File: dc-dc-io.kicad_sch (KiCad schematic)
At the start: 41 parts, among them U20 MPM54304GMN, U28 PAC1944T-E

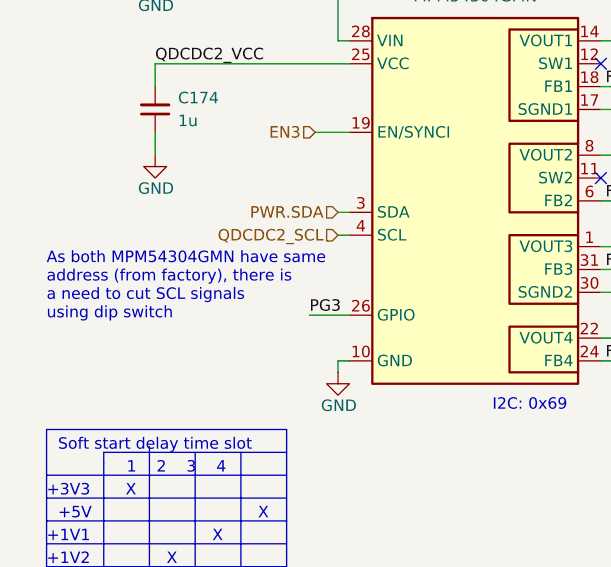
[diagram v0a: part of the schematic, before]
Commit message: [#66727] Continue routing low speed signals
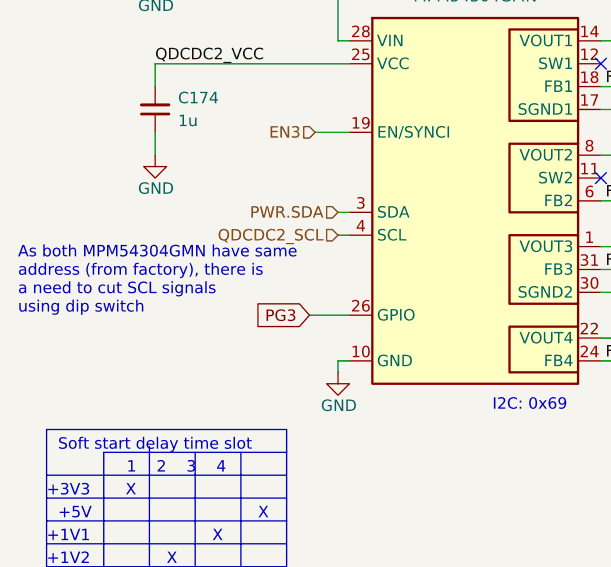
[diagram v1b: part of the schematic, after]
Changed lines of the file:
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@@
   )
   (text "As both MPM54304GMN have same \naddress (from factory), there is \na need to cut SCL signals\nusing dip switch"
-    (at 57.15 113.03 0)
+    (at 53.975 112.395 0)
     (effects (font (size 1.27 1.27)) (justify left bottom))
   )
@@
     (effects (font (size 1.27 1.27)) (justify right bottom))
   )
-  (label "PG3" (at 86.36 112.395 0) (fields_autoplaced)
-    (effects (font (size 1.27 1.27)) (justify left bottom))
-  )
   (label "5V_SEN_+" (at 149.86 174.625 180) (fields_autoplaced)
     (effects (font (size 1.27 1.27)) (justify right bottom))
@@
     (effects (font (size 1.27 1.27)) (justify left bottom))
   )
+  (global_label "PG3" (shape input) (at 86.36 112.395 180) (fields_autoplaced)
+    (effects (font (size 1.27 1.27)) (justify right))
+    (property "Intersheetrefs" "${INTERSHEET_REFS}" (at 80.2795 112.395 0)
+      (effects (font (size 1.27 1.27)) (justify right))
+    )
+  )
   (hierarchical_label "PWR.SCL" (shape input) (at 100.33 172.085 180) (fields_autoplaced)

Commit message: [#67725] Update vccio power supply
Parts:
- C193: DNP DNP -> (none)
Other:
- note added: "1"
- note added: "Current sense monitor"
- note removed: "1 2 3 4"
- moved on the sheet: C173, C174, C178, C184, C185, C190, C191, C192, C193, C206, R145, R146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

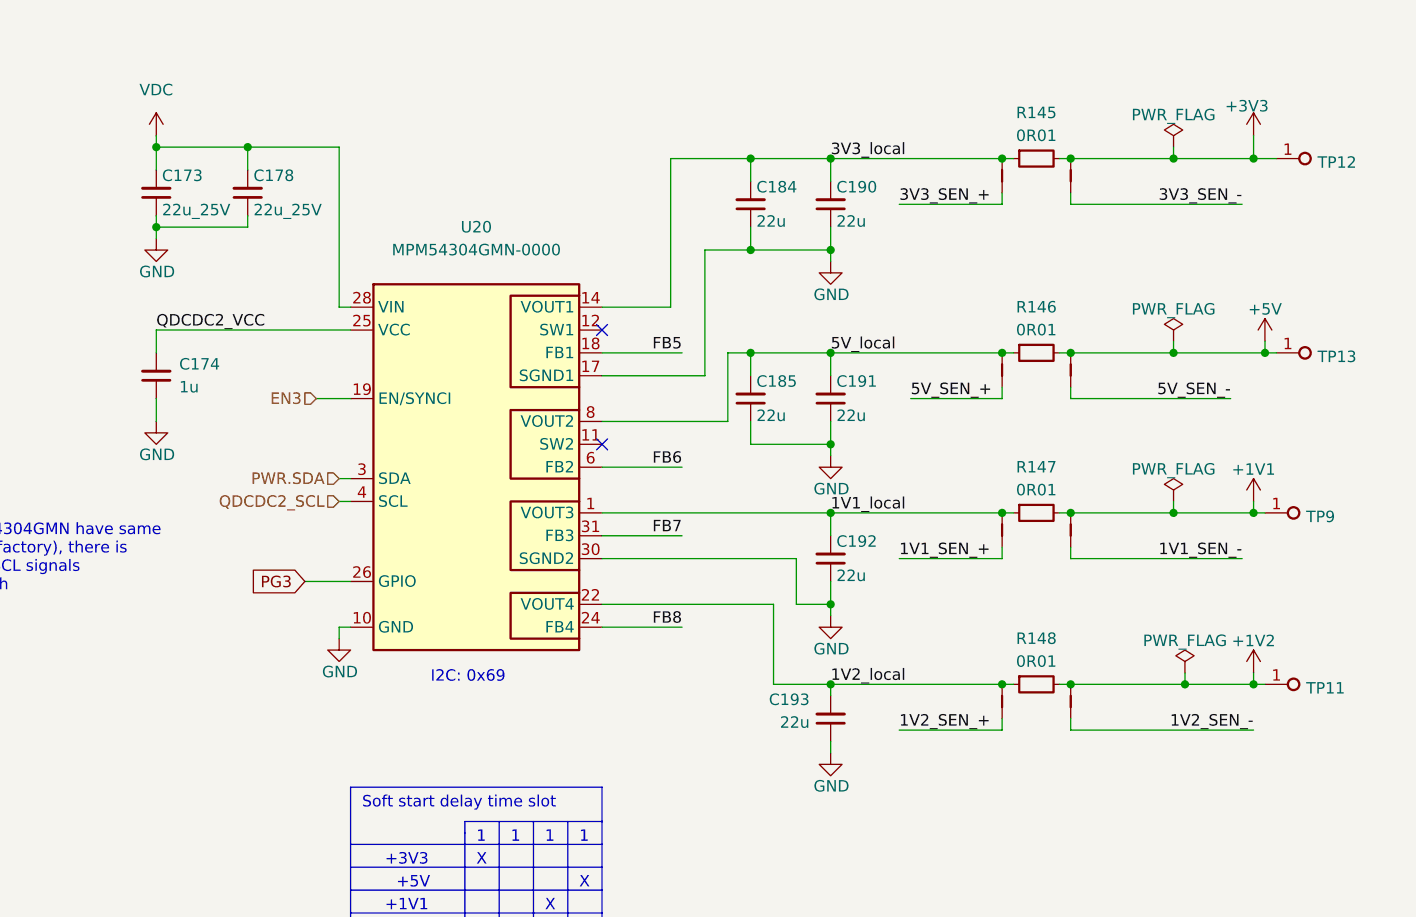
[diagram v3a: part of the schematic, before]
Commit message: [#68016] Solve ERC warrings and errors
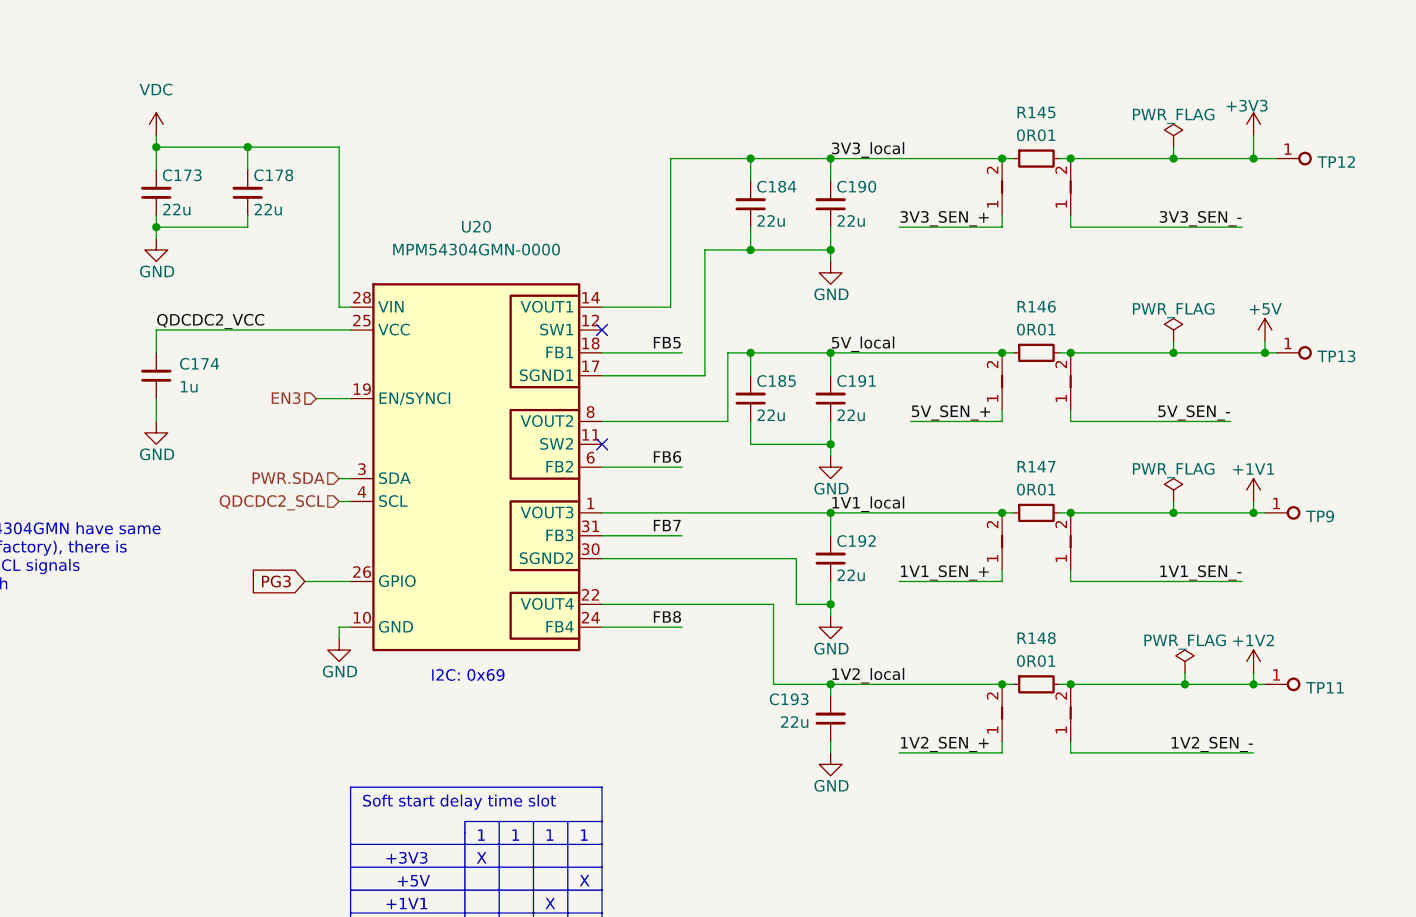
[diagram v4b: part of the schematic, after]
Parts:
- C173, C178: Dielectric (none) -> X5R; Public (none) -> False; Val 22u_25V -> 22u; Voltage (none) -> 25V
